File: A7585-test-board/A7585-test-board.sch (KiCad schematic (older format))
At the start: 25 parts, among them J100 Conn_Coaxial_Power, SW201 SW_SPDT, SW302 SW_Push_SPDT, SW303 SW_Push_SPDT, U100 MPM3610, U200 A7585D, U300 Pico

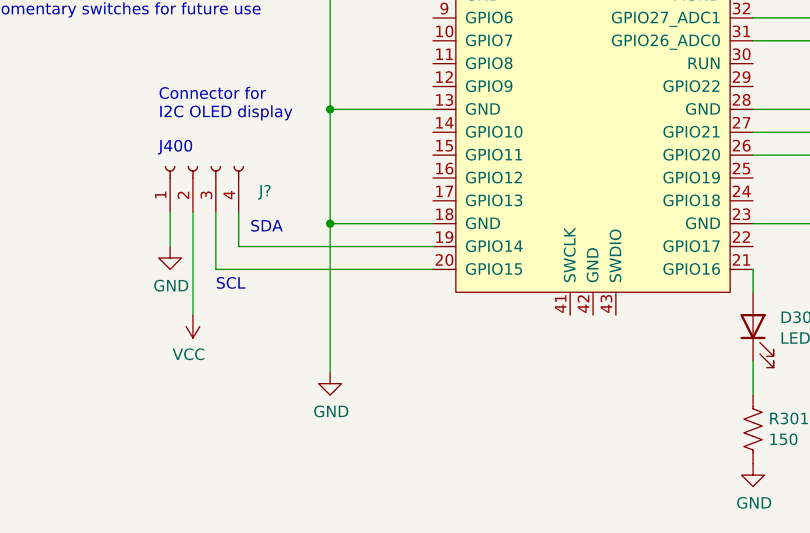
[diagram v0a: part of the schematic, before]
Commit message: Minor change to schematic.
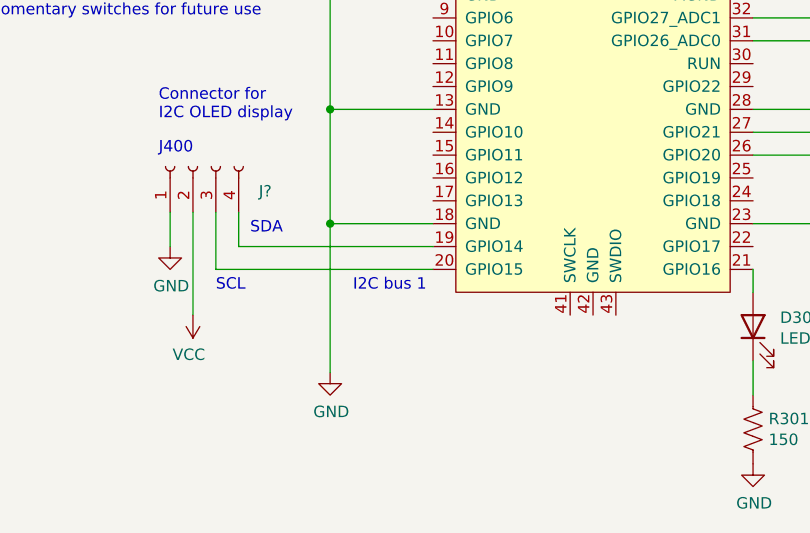
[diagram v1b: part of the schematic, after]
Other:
- note added: "I2C bus 1"
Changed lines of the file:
@@
 Text Notes 3400 5400 0    50   ~ 0
 Connector for \nI2C OLED display
+Text Notes 4250 6150 0    50   ~ 0
+I2C bus 1
 $EndSCHEMATC
